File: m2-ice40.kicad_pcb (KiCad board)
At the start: 2 copper layers, 30 x 38 mm, 73 parts, among them J601 m.2_socket2_module, U201 93LC56C-I/SN, U202 FT2232H, U301 ICE40HX1K-TQ144, U401 W25Q80DVSNIG, U701 MAX6621, X201 DSC6001JI2A-012.0000

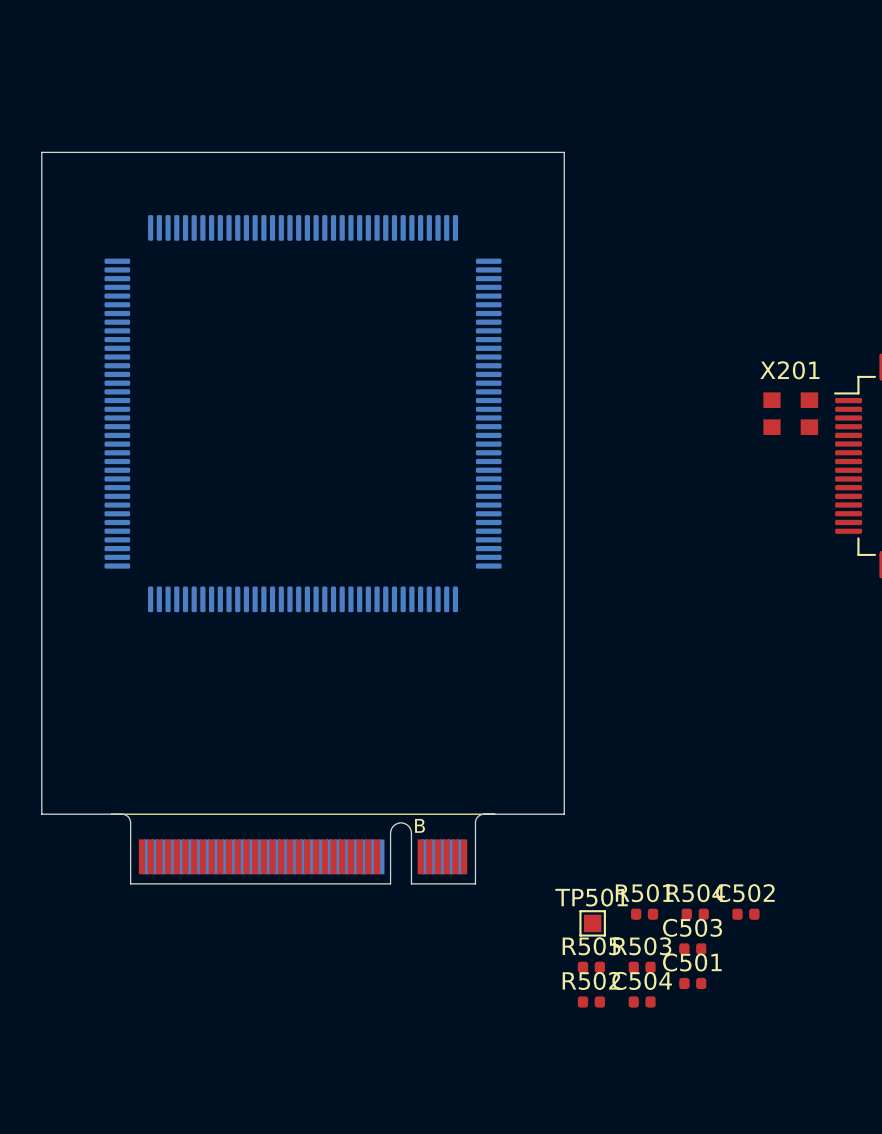
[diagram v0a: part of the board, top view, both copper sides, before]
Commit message: added a couple more footprints
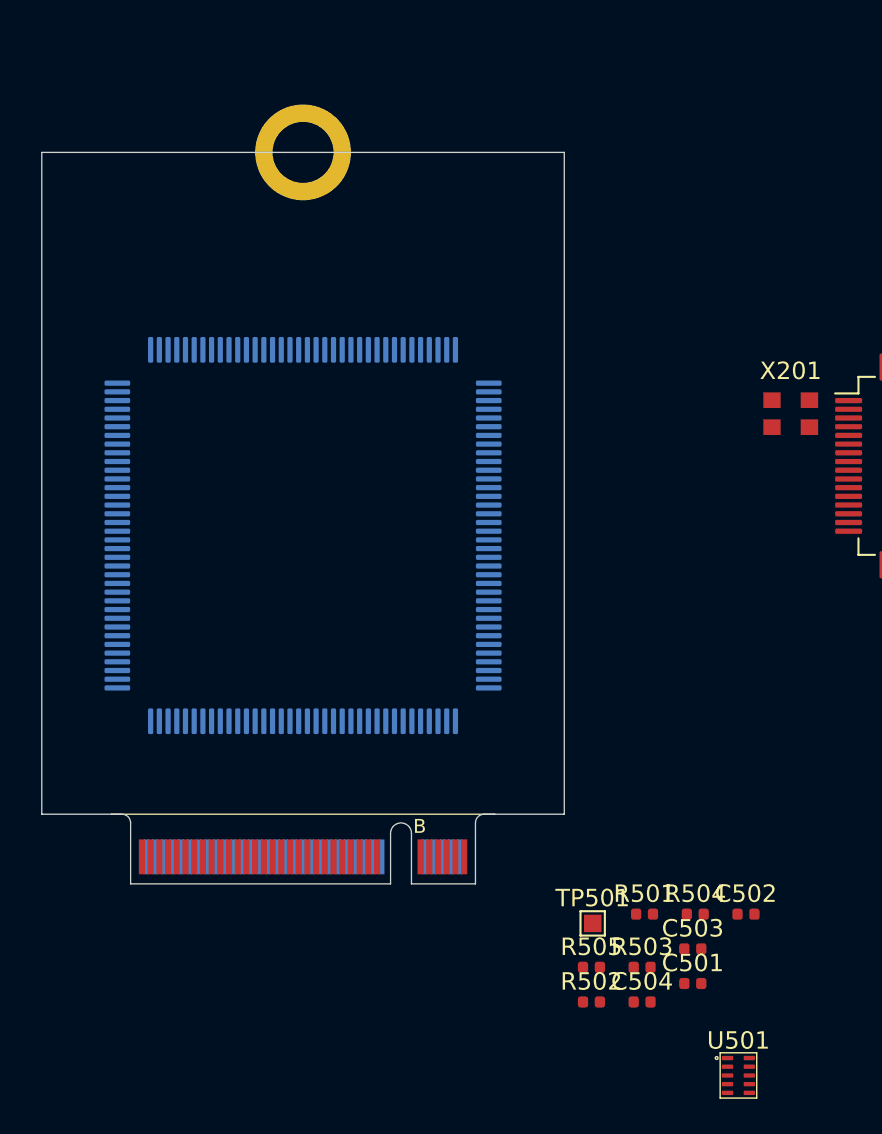
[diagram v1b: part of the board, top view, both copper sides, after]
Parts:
- added J602: M.2-GND-MOUNTING, m2-ice40:m.2_mechanical_ground_pad, F.Cu at (115.0, 58.0)
- added U501: TPSM82821, m2-ice40:SIL0010D, F.Cu at (140.0, 111.0)
- moved U301 7.00 mm to (115.0, 80.0)
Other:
- outline, holes or cut-outs redrawn
- copper layers 2 -> 4
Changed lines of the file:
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@@
 (kicad_pcb (version 20171130) (host pcbnew 5.1.4+dfsg1-1)
   (general
-    (thickness 1.6)
+    (thickness 0.8)
     (drawings 5)
     (tracks 0)
     (zones 0)
-    (modules 73)
+    (modules 75)
     (nets 242)
   )
@@
   (layers
     (0 F.Cu signal)
+    (1 In1.Cu signal)
+    (2 In2.Cu signal)
     (31 B.Cu signal)
     (32 B.Adhes user)
@@
     (46 B.CrtYd user)
     (47 F.CrtYd user)
-    (48 B.Fab user hide)
-    (49 F.Fab user hide)
+    (48 B.Fab user)
+    (49 F.Fab user)
   )
   (setup
@@
     (add_net "Net-(U301-Pad99)")
   )
+  (module m2-ice40:SIL0010D (layer F.Cu)
+    (at 140 111)
+    (fp_text reference U501 (at 0 -2) (layer F.SilkS)
+      (effects (font (size 1 1) (thickness 0.15)))
+    )
+    (fp_text value TPSM82821 (at 0 2) (layer F.Fab)
+      (effects (font (size 1 1) (thickness 0.15)))
+    )
+    (fp_circle (center -1.25 -1) (end -1.17 -1) (layer F.SilkS) (width 0.08))
+    (fp_line (start -1.05 1.3) (end -1.05 -1.3) (layer F.SilkS) (width 0.08))
+    (fp_line (start 1.05 1.3) (end -1.05 1.3) (layer F.SilkS) (width 0.08))
+    (fp_line (start 1.05 -1.3) (end 1.05 1.3) (layer F.SilkS) (width 0.08))
+    (fp_line (start -1.05 -1.3) (end 1.05 -1.3) (layer F.SilkS) (width 0.08))
+    (pad 10 smd roundrect (at 0.625 -1) (size 0.65 0.25) (layers F.Cu F.Paste F.Mask) (roundrect_rratio 0.2)
+      (net 7 "Net-(C501-Pad2)"))
+    (pad 9 smd roundrect (at 0.625 -0.5) (size 0.65 0.25) (layers F.Cu F.Paste F.Mask) (roundrect_rratio 0.2)
+      (net 7 "Net-(C501-Pad2)"))
+    (pad 8 smd roundrect (at 0.625 0) (size 0.65 0.25) (layers F.Cu F.Paste F.Mask) (roundrect_rratio 0.2)
+      (net 8 "Net-(C502-Pad2)"))
+    (pad 7 smd roundrect (at 0.625 0.5) (size 0.65 0.25) (layers F.Cu F.Paste F.Mask) (roundrect_rratio 0.2)
+      (net 6 "/fpga power and config/1.2V"))
+    (pad 6 smd roundrect (at 0.625 1) (size 0.65 0.25) (layers F.Cu F.Paste F.Mask) (roundrect_rratio 0.2)
+      (net 6 "/fpga power and config/1.2V"))
+    (pad 5 smd roundrect (at -0.625 1) (size 0.65 0.25) (layers F.Cu F.Paste F.Mask) (roundrect_rratio 0.2)
+      (net 6 "/fpga power and config/1.2V"))
+    (pad 4 smd roundrect (at -0.625 0.5) (size 0.65 0.25) (layers F.Cu F.Paste F.Mask) (roundrect_rratio 0.2)
+      (net 50 "Net-(R503-Pad2)"))
+    (pad 3 smd roundrect (at -0.625 0) (size 0.65 0.25) (layers F.Cu F.Paste F.Mask) (roundrect_rratio 0.2)
+      (net 2 "/fpga power and config/3.3V"))
+    (pad 2 smd roundrect (at -0.625 -0.5) (size 0.65 0.25) (layers F.Cu F.Paste F.Mask) (roundrect_rratio 0.2)
+      (net 2 "/fpga power and config/3.3V"))
+    (pad 1 smd roundrect (at -0.625 -1) (size 0.65 0.25) (layers F.Cu F.Paste F.Mask) (roundrect_rratio 0.2)
+      (net 2 "/fpga power and config/3.3V"))
+  )
+  (module m2-ice40:m.2_mechanical_ground_pad (layer F.Cu)
+    (at 115 58)
+    (fp_text reference J602 (at 0 5) (layer F.SilkS) hide
+      (effects (font (size 1 1) (thickness 0.15)))
+    )
+    (fp_text value M.2-GND-MOUNTING (at 0 -4) (layer F.Fab) hide
+      (effects (font (size 1 1) (thickness 0.15)))
+    )
+    (fp_line (start 2.5 1) (end 2.5 -0.5) (layer B.Mask) (width 1))
+    (fp_line (start -2.5 1) (end -2.5 -0.5) (layer B.Mask) (width 1))
+    (fp_arc (start 0 1) (end -2 1) (angle -180) (layer B.Mask) (width 2))
+    (pad 1 thru_hole circle (at 0 0) (size 5.5 5.5) (drill 3.5) (layers *.Cu *.Mask)
+      (net 1 GND))
+  )
   (module m2ngff:m2-padKeyB (layer F.Cu)
     (at 115 100)
@@
   )
   (module Package_QFP:TQFP-144_20x20mm_P0.5mm (layer B.Cu)
-    (at 115 73)
+    (at 115 80)
     (descr "TQFP, 144 Pin (http://www.microsemi.com/index.php?option=com_docman&task=doc_download&gid=131095), generated with kicad-footprint-generator ipc_qfp_generator.py")
     (tags "TQFP QFP")
@@
   (gr_line (start 100 96) (end 100 58) (layer Edge.Cuts) (width 0.05))
   (gr_line (start 104 96) (end 100 96) (layer Edge.Cuts) (width 0.05))
-  (gr_line (start 130 96) (end 125.4 96) (layer Edge.Cuts) (width 0.05))
+  (gr_line (start 130 96) (end 126 96) (layer Edge.Cuts) (width 0.05))
   (gr_line (start 130 58) (end 130 96) (layer Edge.Cuts) (width 0.05))
   (gr_line (start 100 58) (end 130 58) (layer Edge.Cuts) (width 0.05))

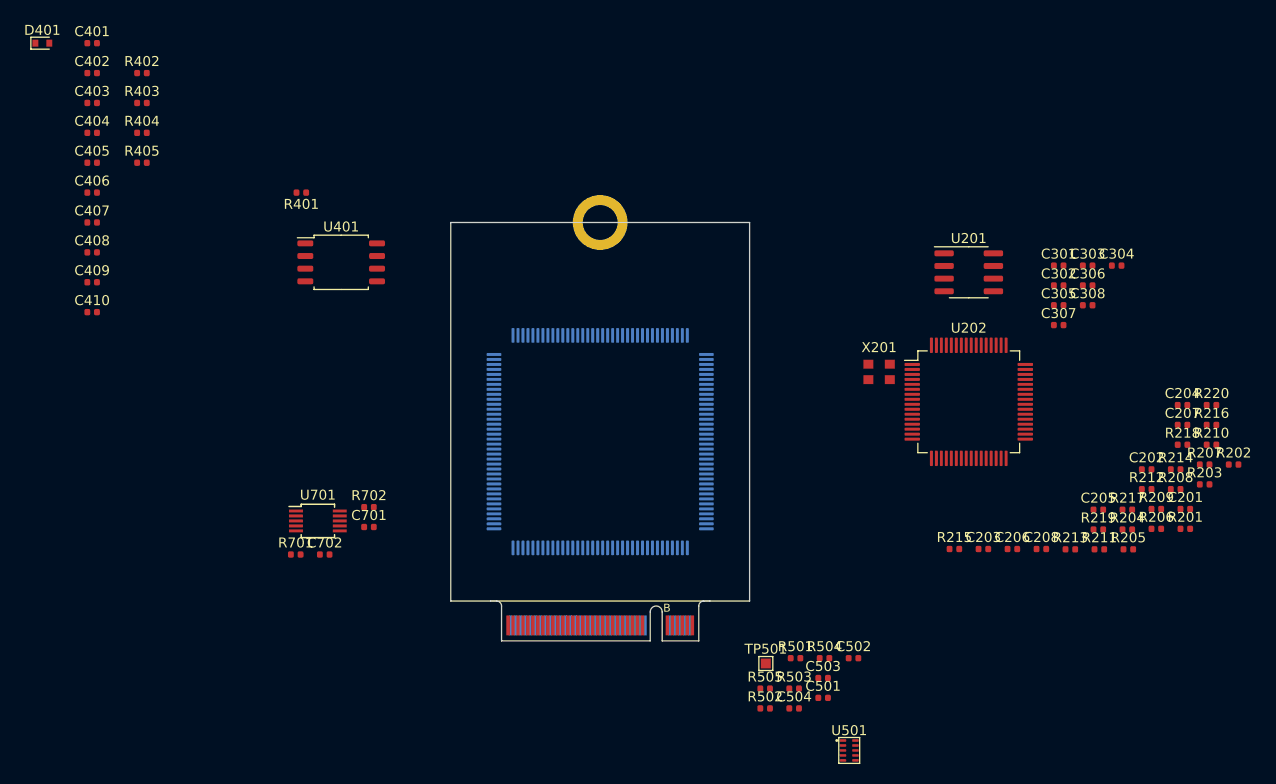
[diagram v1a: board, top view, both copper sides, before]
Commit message: local component placement
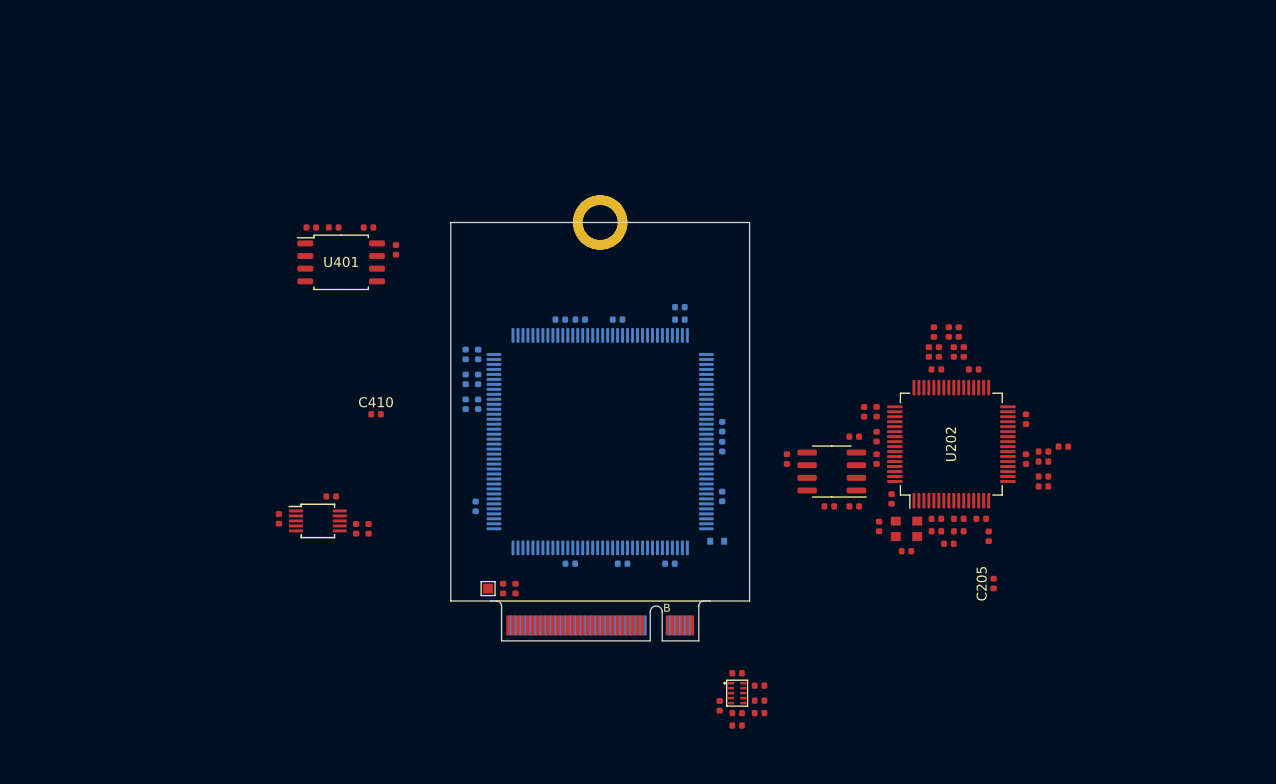
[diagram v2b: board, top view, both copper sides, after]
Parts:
- added C209: 0.1u, Capacitor_SMD:C_0402_1005Metric, F.Cu at (148.8, 72.8)
- added C210: 0.1u, Capacitor_SMD:C_0402_1005Metric, F.Cu at (153.2, 87.8)
- added C211: 0.1u, Capacitor_SMD:C_0402_1005Metric, F.Cu at (157.8, 81.8)
- added C212: 0.1u, Capacitor_SMD:C_0402_1005Metric, F.Cu at (152.5, 72.8)
- added C213: 0.1u, Capacitor_SMD:C_0402_1005Metric, F.Cu at (157.8, 77.8)
- added C214: 0.1u, Capacitor_SMD:C_0402_1005Metric, F.Cu at (144.2, 85.8)
- added C215: 0.1u, Capacitor_SMD:C_0402_1005Metric, F.Cu at (142.8, 79.5)
- C301, C302, C303, C304, C305, C306, C307, C308, C402, C403, C404, C405, C406, C407, C408, C409, D401, R404, R405: moved to B.Cu
- moved D401 84.2 mm to (126.8, 90.0)
- moved C408 66.2 mm to (127.2, 80.5), turned to 90 degrees
- moved C409 64.5 mm to (122.0, 92.2), turned to 180 degrees
- moved C402 64.0 mm to (123.0, 67.8), turned to 180 degrees
- moved C308 61.6 mm to (102.8, 73.8), turned to 90 degrees
- moved C307 61.3 mm to (102.5, 86.5), turned to 270 degrees
- moved C301 57.4 mm to (112.0, 92.2)
- moved R404 56.8 mm to (123.0, 66.5), turned to 180 degrees
- moved C302 51.9 mm to (117.2, 92.2)
- moved C305 50.1 mm to (111.0, 67.8)
- moved C407 50.0 mm to (113.0, 67.8), turned to 180 degrees
- moved C306 47.3 mm to (116.8, 67.8)
- moved C403 46.3 mm to (102.8, 71.2), turned to 270 degrees
- moved C304 45.9 mm to (127.2, 85.5), turned to 270 degrees
- moved C405 45.7 mm to (102.8, 76.2), turned to 270 degrees
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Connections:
- C501 pad 2: Net-(C501-Pad2) -> GND
- C503 pad 2: Net-(C501-Pad2) -> GND
- C504 pad 2: Net-(C501-Pad2) -> GND
- C702 pad 1: /peci/PECI -> /peci/PECI_VREF
- R505 pad 2: Net-(C501-Pad2) -> GND
- U501 pad 10: Net-(C501-Pad2) -> GND
- U501 pad 9: Net-(C501-Pad2) -> GND
- U701 pad 1: /peci/PECI_VREF -> /peci/PECI
- U701 pad 10: /peci/PECI -> /peci/PECI_VREF

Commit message: assigning pins, adding test points, placing stuff, etc
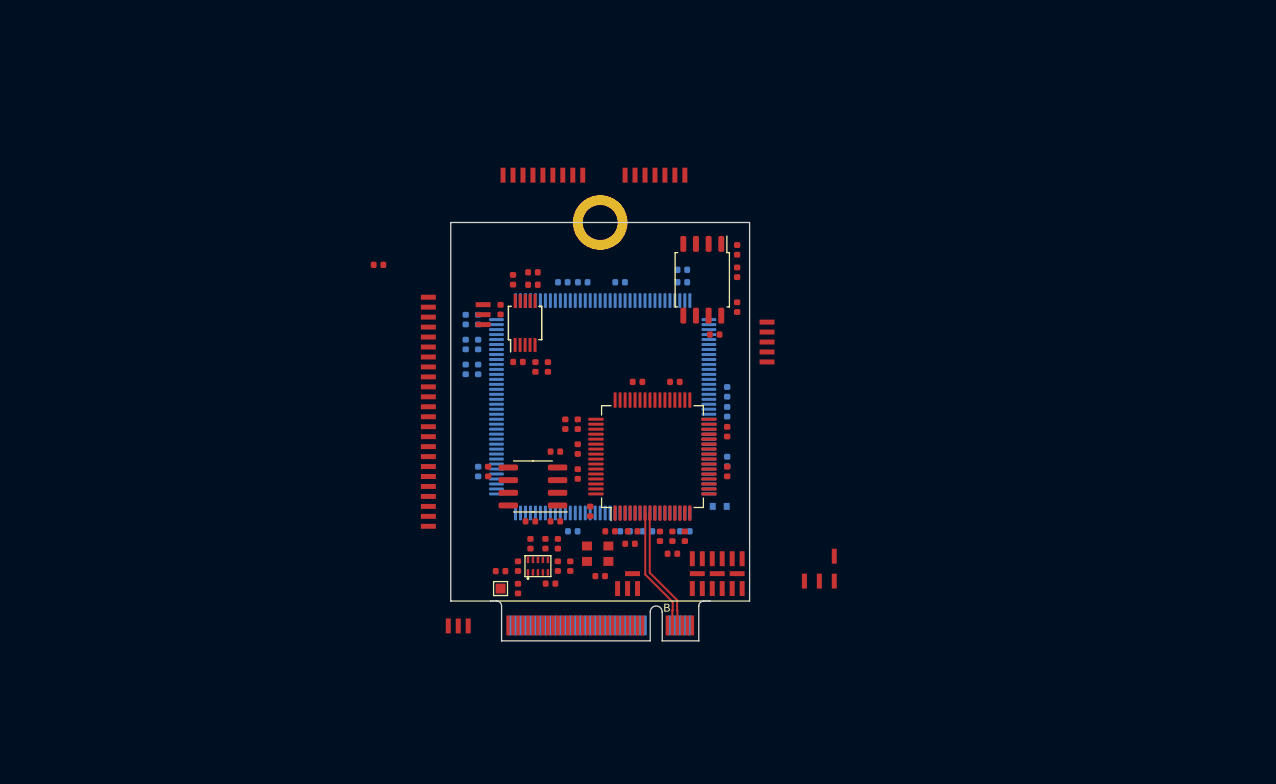
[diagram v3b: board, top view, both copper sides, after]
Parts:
- removed R208, R209, R210, R211, R212, R213, R214, R215, R216, R217, R218, R219, R220: 0, Resistor_SMD:R_0402_1005Metric
- added R703: 2.2k, Resistor_SMD:R_0402_1005Metric, F.Cu at (106.2, 63.8)
- added R704: 2.2k, Resistor_SMD:R_0402_1005Metric, F.Cu at (108.5, 72.5)
- added R705: 2.2k, Resistor_SMD:R_0402_1005Metric, F.Cu at (109.8, 72.5)
- added TP101: PECI_VREF, m2-ice40:TestPoint_Pad_0.5x1.5mm, F.Cu at (103.2, 66.2)
- added TP102: PECI, m2-ice40:TestPoint_Pad_0.5x1.5mm, F.Cu at (103.2, 68.2)
- added TP103: PECI_GND, m2-ice40:TestPoint_Pad_0.5x1.5mm, F.Cu at (103.2, 67.2)
- added TP701: TestPoint, m2-ice40:TestPoint_Pad_0.5x1.5mm, F.Cu at (125.2, 94.8)
- added TP702: TestPoint, m2-ice40:TestPoint_Pad_0.5x1.5mm, F.Cu at (124.2, 94.8)
- added TP703: TestPoint, m2-ice40:TestPoint_Pad_0.5x1.5mm, F.Cu at (125.2, 91.8)
- added TP704: TestPoint, m2-ice40:TestPoint_Pad_0.5x1.5mm, F.Cu at (124.2, 91.8)
- added TP705: TestPoint, m2-ice40:TestPoint_Pad_0.5x1.5mm, F.Cu at (129.2, 94.8)
- added TP706: TestPoint, m2-ice40:TestPoint_Pad_0.5x1.5mm, F.Cu at (128.2, 94.8)
- added TP707: TestPoint, m2-ice40:TestPoint_Pad_0.5x1.5mm, F.Cu at (127.2, 94.8)
- added TP708: TestPoint, m2-ice40:TestPoint_Pad_0.5x1.5mm, F.Cu at (126.2, 94.8)
- added TP709: TestPoint, m2-ice40:TestPoint_Pad_0.5x1.5mm, F.Cu at (118.8, 94.8)
- added TP710: TestPoint, m2-ice40:TestPoint_Pad_0.5x1.5mm, F.Cu at (117.8, 94.8)
- added TP711: TestPoint, m2-ice40:TestPoint_Pad_0.5x1.5mm, F.Cu at (116.8, 94.8)
- added TP712: TestPoint, m2-ice40:TestPoint_Pad_0.5x1.5mm, F.Cu at (101.8, 98.5)
- added TP713: TestPoint, m2-ice40:TestPoint_Pad_0.5x1.5mm, F.Cu at (100.8, 98.5)
- added TP714: TestPoint, m2-ice40:TestPoint_Pad_0.5x1.5mm, F.Cu at (99.8, 98.5)
- added TP715: TestPoint, m2-ice40:TestPoint_Pad_0.5x1.5mm, F.Cu at (131.8, 68.0)
- added TP716: TestPoint, m2-ice40:TestPoint_Pad_0.5x1.5mm, F.Cu at (131.8, 69.0)
- added TP717: TestPoint, m2-ice40:TestPoint_Pad_0.5x1.5mm, F.Cu at (131.8, 70.0)
- added TP718: TestPoint, m2-ice40:TestPoint_Pad_0.5x1.5mm, F.Cu at (131.8, 71.0)
- added TP719: TestPoint, m2-ice40:TestPoint_Pad_0.5x1.5mm, F.Cu at (131.8, 72.0)
- added TP720: TestPoint, m2-ice40:TestPoint_Pad_0.5x1.5mm, F.Cu at (129.2, 91.8)
- added TP721: TestPoint, m2-ice40:TestPoint_Pad_0.5x1.5mm, F.Cu at (128.2, 91.8)
- added TP722: TestPoint, m2-ice40:TestPoint_Pad_0.5x1.5mm, F.Cu at (127.2, 91.8)
- added TP723: TestPoint, m2-ice40:TestPoint_Pad_0.5x1.5mm, F.Cu at (126.2, 91.8)
- added TP724: TestPoint, m2-ice40:TestPoint_Pad_0.5x1.5mm, F.Cu at (105.2, 53.2)
- added TP725: TestPoint, m2-ice40:TestPoint_Pad_0.5x1.5mm, F.Cu at (106.2, 53.2)
- added TP726: TestPoint, m2-ice40:TestPoint_Pad_0.5x1.5mm, F.Cu at (107.2, 53.2)
- added TP727: TestPoint, m2-ice40:TestPoint_Pad_0.5x1.5mm, F.Cu at (108.2, 53.2)
- added TP728: TestPoint, m2-ice40:TestPoint_Pad_0.5x1.5mm, F.Cu at (109.2, 53.2)
- added TP729: TestPoint, m2-ice40:TestPoint_Pad_0.5x1.5mm, F.Cu at (110.2, 53.2)
- added TP730: TestPoint, m2-ice40:TestPoint_Pad_0.5x1.5mm, F.Cu at (111.2, 53.2)
- added TP731: TestPoint, m2-ice40:TestPoint_Pad_0.5x1.5mm, F.Cu at (112.2, 53.2)
- added TP732: TestPoint, m2-ice40:TestPoint_Pad_0.5x1.5mm, F.Cu at (113.2, 53.2)
- added TP733: TestPoint, m2-ice40:TestPoint_Pad_0.5x1.5mm, F.Cu at (117.5, 53.2)
- added TP734: TestPoint, m2-ice40:TestPoint_Pad_0.5x1.5mm, F.Cu at (118.5, 53.2)
- added TP735: TestPoint, m2-ice40:TestPoint_Pad_0.5x1.5mm, F.Cu at (119.5, 53.2)
- added TP736: TestPoint, m2-ice40:TestPoint_Pad_0.5x1.5mm, F.Cu at (120.5, 53.2)
- added TP737: TestPoint, m2-ice40:TestPoint_Pad_0.5x1.5mm, F.Cu at (121.5, 53.2)
- added TP738: TestPoint, m2-ice40:TestPoint_Pad_0.5x1.5mm, F.Cu at (122.5, 53.2)
- added TP739: TestPoint, m2-ice40:TestPoint_Pad_0.5x1.5mm, F.Cu at (123.5, 53.2)
- added TP740: TestPoint, m2-ice40:TestPoint_Pad_0.5x1.5mm, F.Cu at (97.8, 88.5)
- added TP741: TestPoint, m2-ice40:TestPoint_Pad_0.5x1.5mm, F.Cu at (97.8, 87.5)
- added TP742: TestPoint, m2-ice40:TestPoint_Pad_0.5x1.5mm, F.Cu at (97.8, 86.5)
- added TP743: TestPoint, m2-ice40:TestPoint_Pad_0.5x1.5mm, F.Cu at (97.8, 85.5)
- added TP744: TestPoint, m2-ice40:TestPoint_Pad_0.5x1.5mm, F.Cu at (97.8, 84.5)
- added TP745: TestPoint, m2-ice40:TestPoint_Pad_0.5x1.5mm, F.Cu at (97.8, 83.5)
- added TP746: TestPoint, m2-ice40:TestPoint_Pad_0.5x1.5mm, F.Cu at (97.8, 82.5)
- added TP747: TestPoint, m2-ice40:TestPoint_Pad_0.5x1.5mm, F.Cu at (97.8, 81.5)
- added TP748: TestPoint, m2-ice40:TestPoint_Pad_0.5x1.5mm, F.Cu at (97.8, 80.5)
- added TP749: TestPoint, m2-ice40:TestPoint_Pad_0.5x1.5mm, F.Cu at (97.8, 79.5)
- added TP750: TestPoint, m2-ice40:TestPoint_Pad_0.5x1.5mm, F.Cu at (97.8, 78.5)
- added TP751: TestPoint, m2-ice40:TestPoint_Pad_0.5x1.5mm, F.Cu at (97.8, 77.5)
- added TP752: TestPoint, m2-ice40:TestPoint_Pad_0.5x1.5mm, F.Cu at (97.8, 76.5)
- added TP753: TestPoint, m2-ice40:TestPoint_Pad_0.5x1.5mm, F.Cu at (97.8, 75.5)
- added TP754: TestPoint, m2-ice40:TestPoint_Pad_0.5x1.5mm, F.Cu at (97.8, 74.5)
- added TP755: TestPoint, m2-ice40:TestPoint_Pad_0.5x1.5mm, F.Cu at (97.8, 73.5)
- added TP756: TestPoint, m2-ice40:TestPoint_Pad_0.5x1.5mm, F.Cu at (97.8, 72.5)
- added TP757: TestPoint, m2-ice40:TestPoint_Pad_0.5x1.5mm, F.Cu at (97.8, 71.5)
- added TP758: TestPoint, m2-ice40:TestPoint_Pad_0.5x1.5mm, F.Cu at (97.8, 70.5)
- added TP759: TestPoint, m2-ice40:TestPoint_Pad_0.5x1.5mm, F.Cu at (97.8, 69.5)
- added TP760: TestPoint, m2-ice40:TestPoint_Pad_0.5x1.5mm, F.Cu at (97.8, 68.5)
- added TP761: TestPoint, m2-ice40:TestPoint_Pad_0.5x1.5mm, F.Cu at (97.8, 67.5)
- added TP762: TestPoint, m2-ice40:TestPoint_Pad_0.5x1.5mm, F.Cu at (97.8, 66.5)
- added TP763: TestPoint, m2-ice40:TestPoint_Pad_0.5x1.5mm, F.Cu at (97.8, 65.5)
- added TP764: TestPoint, m2-ice40:TestPoint_Pad_0.5x1.5mm, F.Cu at (128.8, 93.2)
- added TP765: TestPoint, m2-ice40:TestPoint_Pad_0.5x1.5mm, F.Cu at (124.8, 93.2)
- added TP766: TestPoint, m2-ice40:TestPoint_Pad_0.5x1.5mm, F.Cu at (126.8, 93.2)
- added TP767: TestPoint, m2-ice40:TestPoint_Pad_0.5x1.5mm, F.Cu at (118.2, 93.2)
- added TP768: TestPoint, m2-ice40:TestPoint_Pad_0.5x1.5mm, F.Cu at (138.5, 91.5)
- added TP769: TestPoint, m2-ice40:TestPoint_Pad_0.5x1.5mm, F.Cu at (135.5, 94.0)
- added TP770: TestPoint, m2-ice40:TestPoint_Pad_0.5x1.5mm, F.Cu at (137.0, 94.0)
- added TP771: TestPoint, m2-ice40:TestPoint_Pad_0.5x1.5mm, F.Cu at (138.5, 94.0)
- R205: moved to B.Cu
- R405: value 10k -> 100
- moved R401 42.8 mm to (128.8, 60.8), turned to 90 degrees
- moved R403 40.7 mm to (128.8, 63.0), turned to 90 degrees
- moved C401 37.9 mm to (128.8, 66.5), turned to 90 degrees
- moved U401 36.3 mm to (125.2, 63.8), turned to 270 degrees
- moved R402 33.1 mm to (126.5, 69.2), turned to 0 degrees
- moved C205 32.4 mm to (122.2, 91.2), turned to 180 degrees
- moved C206 32.0 mm to (118.0, 90.2), turned to 0 degrees
- moved X201 31.1 mm to (114.8, 91.2)
- moved C210 31.0 mm to (122.2, 89.5), turned to 270 degrees
- moved C202 30.9 mm to (115.0, 93.5)
- moved R701 30.6 mm to (108.2, 63.0), turned to 0 degrees
- moved C208 30.5 mm to (118.2, 89.0)
- moved C214 30.3 mm to (114.0, 87.0)
- moved C701 30.3 mm to (108.2, 64.2), turned to 180 degrees
- moved C207 30.1 mm to (121.0, 89.5), turned to 270 degrees
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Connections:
- R202 pad 1: /ftdi/ICE_CLK -> /FPGA/ICE_CLK
- U202 pad 16: /ftdi/FTDI_SCK -> /FPGA/FTDI_TX__ICE_RX
- U202 pad 17: /ftdi/FTDI_SI -> /FPGA/FTDI_RX__ICE_TX
- U202 pad 18: /ftdi/FTDI_SO -> /FPGA/FTDI_RTS
- U202 pad 19: Net-(U202-Pad19) -> /FPGA/FTDI_CTS
- U202 pad 21: /ftdi/FTDI_SS -> /FPGA/FTDI_DTR
- U202 pad 22: Net-(U202-Pad22) -> /FPGA/FTDI_DSR
- U202 pad 23: Net-(R212-Pad2) -> /FPGA/FTDI_DCD
- U202 pad 24: Net-(R213-Pad2) -> /FPGA/ADBUS7
- U202 pad 26: Net-(U202-Pad26) -> /FPGA/ACBUS0
- U202 pad 27: Net-(U202-Pad27) -> /FPGA/ACBUS1
- U202 pad 28: Net-(U202-Pad28) -> /FPGA/ACBUS2
- U202 pad 29: Net-(U202-Pad29) -> /FPGA/ACBUS3
- U202 pad 30: Net-(U202-Pad30) -> /FPGA/ACBUS4
- U202 pad 32: Net-(U202-Pad32) -> /FPGA/ACBUS5
- U202 pad 33: Net-(U202-Pad33) -> /FPGA/ACBUS6
- U202 pad 34: Net-(U202-Pad34) -> /FPGA/ACBUS7
- U202 pad 38: Net-(R214-Pad2) -> /ftdi/ICE_SCK
- U202 pad 39: Net-(R215-Pad2) -> /ftdi/ICE_MOSI
- U202 pad 40: Net-(R216-Pad2) -> /ftdi/ICE_MISO
- U202 pad 43: Net-(R218-Pad2) -> /ftdi/ICE_SS_B
- U202 pad 45: Net-(R220-Pad2) -> /fpga power and config/CDONE
- U202 pad 46: Net-(U202-Pad46) -> /fpga power and config/CRESET
- U301 pad 101: Net-(U301-Pad101) -> /FPGA/FTDI_DSR
- U301 pad 102: Net-(U301-Pad102) -> /FPGA/FTDI_DTR
- U301 pad 104: Net-(U301-Pad104) -> /FPGA/FTDI_CTS
- U301 pad 105: Net-(U301-Pad105) -> /FPGA/FTDI_RTS
- U301 pad 106: Net-(U301-Pad106) -> /FPGA/FTDI_RX__ICE_TX
- U301 pad 107: Net-(U301-Pad107) -> /FPGA/FTDI_TX__ICE_RX
- U301 pad 120: Net-(U301-Pad120) -> /FPGA/POWER_OFF#
- U301 pad 121: Net-(U301-Pad121) -> /FPGA/DISABLE#
- U301 pad 129: Net-(U301-Pad129) -> /FPGA/ICE_CLK
- U301 pad 135: Net-(U301-Pad135) -> /FPGA/UIM_RESET
- U301 pad 136: Net-(U301-Pad136) -> /FPGA/UIM_CLK
- U301 pad 137: Net-(U301-Pad137) -> /FPGA/UIM_DATA
- U301 pad 138: Net-(U301-Pad138) -> /FPGA/UIM_PWR
- U301 pad 139: Net-(U301-Pad139) -> /FPGA/1.8v_OD_SIM_DETECT
- U301 pad 141: Net-(U301-Pad141) -> /FPGA/RESET#
- U301 pad 38: Net-(U301-Pad38) -> /peci/ALERT#
- U301 pad 39: Net-(U301-Pad39) -> /FPGA/PECI_RESET#
- U301 pad 41: Net-(U301-Pad41) -> /FPGA/PECI_SDA
- U301 pad 42: Net-(U301-Pad42) -> /FPGA/PECI_SCL
- U301 pad 81: Net-(U301-Pad81) -> /FPGA/ACBUS7
- U301 pad 87: Net-(U301-Pad87) -> /FPGA/ACBUS6
- U301 pad 88: Net-(U301-Pad88) -> /FPGA/ACBUS5
- U301 pad 90: Net-(U301-Pad90) -> /FPGA/ACBUS4
- U301 pad 91: Net-(U301-Pad91) -> /FPGA/ACBUS3
- U301 pad 95: Net-(U301-Pad95) -> /FPGA/ACBUS2
- U301 pad 96: Net-(U301-Pad96) -> /FPGA/ACBUS1
- U301 pad 97: Net-(U301-Pad97) -> /FPGA/ACBUS0
- U301 pad 98: Net-(U301-Pad98) -> /FPGA/ADBUS7
- U301 pad 99: Net-(U301-Pad99) -> /FPGA/FTDI_DCD
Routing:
- net /ftdi/USB_D-: track 0.00 -> 12.4 mm
- net /ftdi/USB_D+: track 0.00 -> 12.4 mm
